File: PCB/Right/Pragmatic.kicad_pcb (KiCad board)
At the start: 2 copper layers, 114.3 x 123.8 mm, 75 parts, among them J1 Conn_02x07_Odd_Even, SW1 SW_Push, SW10 SW_Push, SW11 SW_Push, SW12 SW_Push, SW13 SW_Push, SW14 SW_Push, SW15 SW_Push, SW16 SW_Push, SW17 SW_Push, SW18 SW_Push, SW19 SW_Push, SW2 SW_Push, SW20 SW_Push, SW21 SW_Push, SW22 SW_Push, SW23 SW_Push, SW24 SW_Push, SW25 SW_Push, SW26 SW_Push, SW27 SW_Push, SW28 SW_Push, SW29 SW_Push, SW3 SW_Push, SW30 SW_Push, SW31 SW_Push, SW32 SW_Push, SW33 SW_Push, SW34 SW_Push, SW35 SW_Push, SW36 SW_Push, SW4 SW_Push, SW5 SW_Push, SW6 SW_Push, SW7 SW_Push, SW8 SW_Push, SW9 SW_Push

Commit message: right
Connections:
- SW1 pad 2: Col12 -> Col7
- SW10 pad 2: Col9 -> Col10
- SW11 pad 2: Col8 -> Col11
- SW12 pad 2: Col7 -> Col12
- SW13 pad 2: Col12 -> Col7
- SW14 pad 2: Col11 -> Col8
- SW15 pad 2: Col10 -> Col9
- SW16 pad 2: Col9 -> Col10
- SW17 pad 2: Col8 -> Col11
- SW18 pad 2: Col7 -> Col12
- SW19 pad 2: Col12 -> Col7
- SW2 pad 2: Col11 -> Col8
- SW20 pad 2: Col11 -> Col8
- SW21 pad 2: Col10 -> Col9
- SW22 pad 2: Col9 -> Col10
- SW23 pad 2: Col8 -> Col11
- SW24 pad 2: Col7 -> Col12
- SW25 pad 2: Col12 -> Col7
- SW26 pad 2: Col11 -> Col8
- SW27 pad 2: Col10 -> Col9
- SW28 pad 2: Col9 -> Col10
- SW29 pad 2: Col8 -> Col11
- SW3 pad 2: Col10 -> Col9
- SW30 pad 2: Col7 -> Col12
- SW31 pad 2: Col12 -> Col7
- SW32 pad 2: Col11 -> Col8
- SW33 pad 2: Col10 -> Col9
- SW34 pad 2: Col9 -> Col10
- SW35 pad 2: Col8 -> Col11
- SW36 pad 2: Col7 -> Col12
- SW4 pad 2: Col9 -> Col10
- SW5 pad 2: Col8 -> Col11
- SW6 pad 2: Col7 -> Col12
- SW7 pad 2: Col12 -> Col7
- SW8 pad 2: Col11 -> Col8
- SW9 pad 2: Col10 -> Col9
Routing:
- net Col11: track 147.1 -> 170.6 mm
- net Col12: track 164.8 -> 182.7 mm
- net Col8: track 164.3 -> 150.5 mm, vias 1 -> 0
- net Col9: track 148.6 -> 135.5 mm, vias 1 -> 0
- net Row2: track 137.0 -> 125.3 mm, vias 3 -> 2
- net Col10: track 133.0 -> 143.7 mm, vias 0 -> 1
- net Row1: track 110.2 -> 120.1 mm, vias 3 -> 0
- net Row3: track 152.4 -> 147.0 mm
- net Row4: track 166.6 -> 161.2 mm
- net Col7: track 181.1 -> 176.0 mm
- net Row5: track 184.4 -> 187.6 mm
- net Row6: track 202.6 -> 199.9 mm, vias 1 -> 0
- net Ground: track 17.5 -> 18.0 mm

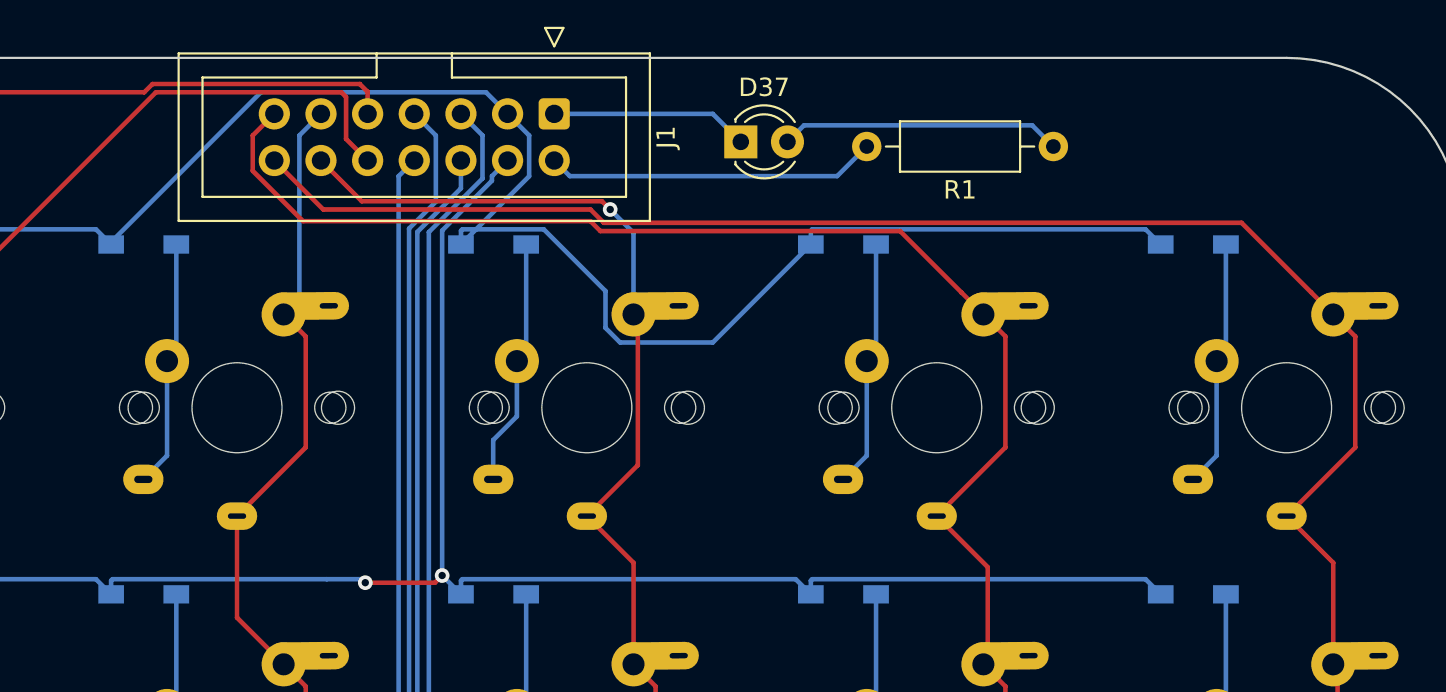
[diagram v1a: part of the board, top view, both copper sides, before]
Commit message: fix power track width
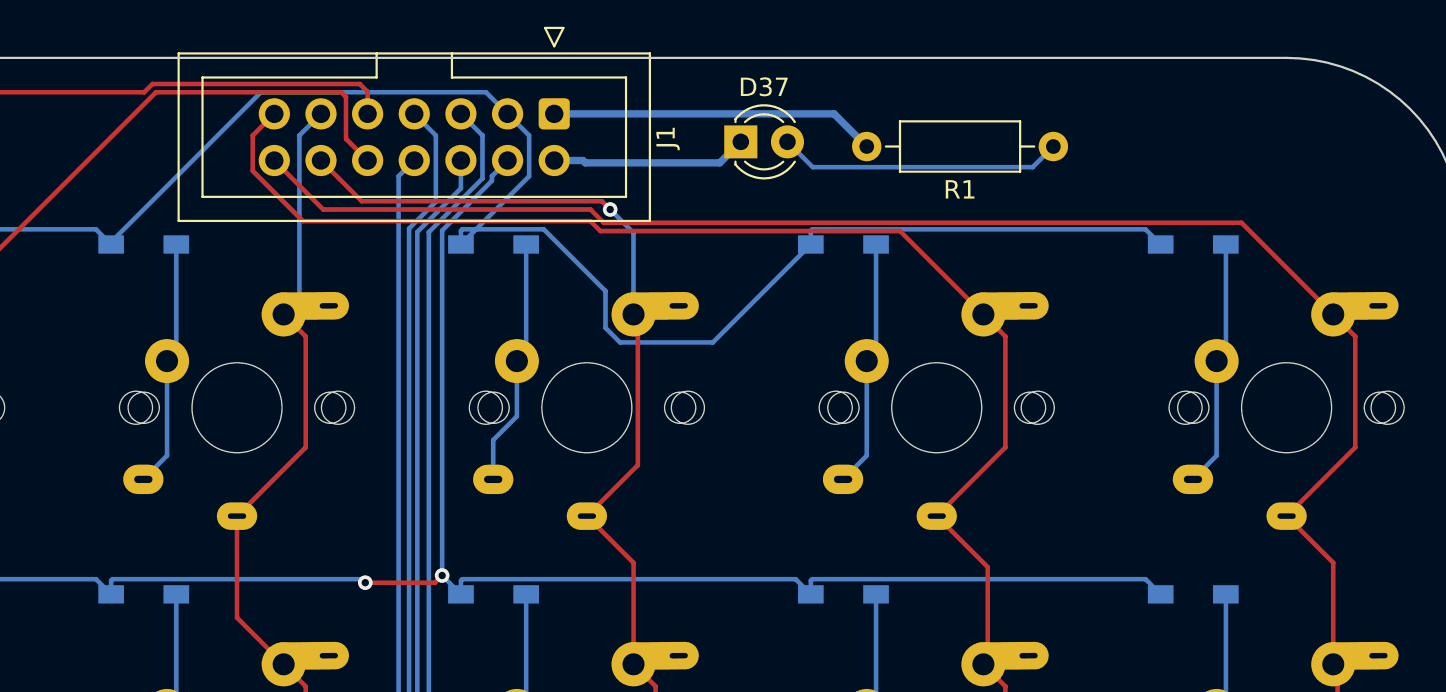
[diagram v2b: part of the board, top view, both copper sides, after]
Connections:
- D37 pad 1: VCC -> Ground
- R1 pad 2: Ground -> VCC
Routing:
- net Ground: track 18.0 -> 10.7 mm
- net VCC: track 10.8 -> 17.8 mm
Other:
- net class Power added: clearance 0.2, trace_width 0.4, via_dia 0.8, via_drill 0.4

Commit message: finish up
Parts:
- added REF**: Logo, Pragmatic:Logo, F.Cu at (76.2, 40.6)
- D37: value LED -> Power
- moved J1 38.0 mm to (150.5, 40.0)
- moved R1 20.4 mm to (119.4, 41.3)
- moved D37 3.94 mm to (126.4, 41.3), turned to 180 degrees
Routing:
- net Col8: track 150.5 -> 189.5 mm
- net Col7: track 176.0 -> 212.3 mm
- net Col9: track 135.5 -> 171.4 mm
- net Col12: track 182.7 -> 147.8 mm
- net Col11: track 170.6 -> 137.3 mm
- net VCC: track 17.8 -> 44.6 mm
- net Ground: track 10.7 -> 32.4 mm
- net Net-(D37-Pad2): track 15.5 -> 4.45 mm
- net Row6: track 199.9 -> 206.7 mm
- net Row3: track 147.0 -> 153.4 mm, vias 2 -> 4
- net Col10: track 143.7 -> 149.6 mm, vias 1 -> 0
- net Row4: track 161.2 -> 166.8 mm, vias 2 -> 4
- net Row1: track 120.1 -> 115.1 mm, vias 0 -> 2
- net Row5: track 187.6 -> 191.9 mm, vias 2 -> 4
- net Row2: track 125.3 -> 129.0 mm, vias 2 -> 4
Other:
- board size 114.3 x 123.8 mm -> 114.3 x 127 mm
- board text added: "Haway"
- board text added: "Pragmatic Kit Right Hand Module Design by James Sa V0.1 2021-11-8"
- board text added: "Right Side"
- board text removed: "Andy"
- board text removed: "Pragmatic"
- board text removed: "Right board v1 2021-11-08 by James Sa"

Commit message: export to gerber
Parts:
- D37: value Power -> LED
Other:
- board text added: "James"
- board text added: "Kai"
